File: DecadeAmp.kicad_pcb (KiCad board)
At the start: 2 copper layers, 60 x 60 mm, 30 parts, among them J1 Conn_Coaxial, J2 Conn_Coaxial, SW1 SS-24E06-TG 5 (P), U1 MCP6292-E/SN, U2 MCP6292-E/SN

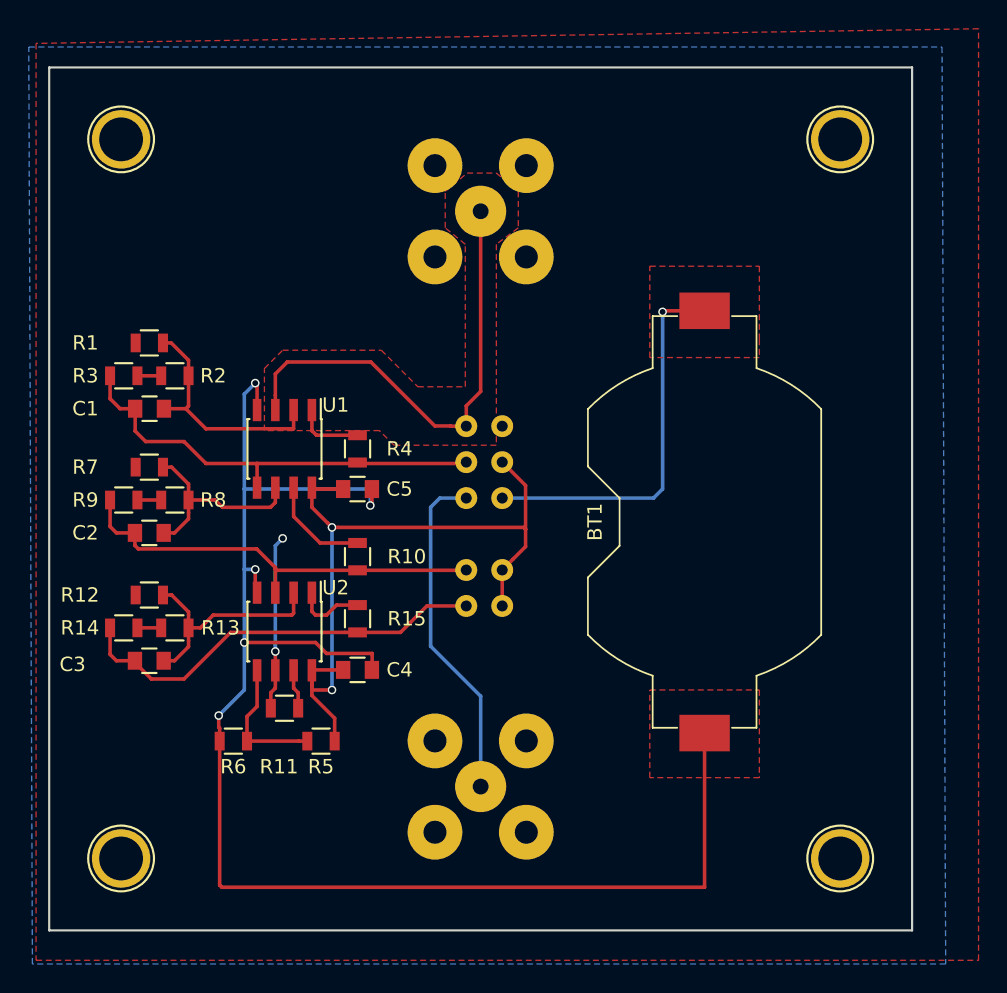
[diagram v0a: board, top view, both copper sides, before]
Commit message: moved to new packages
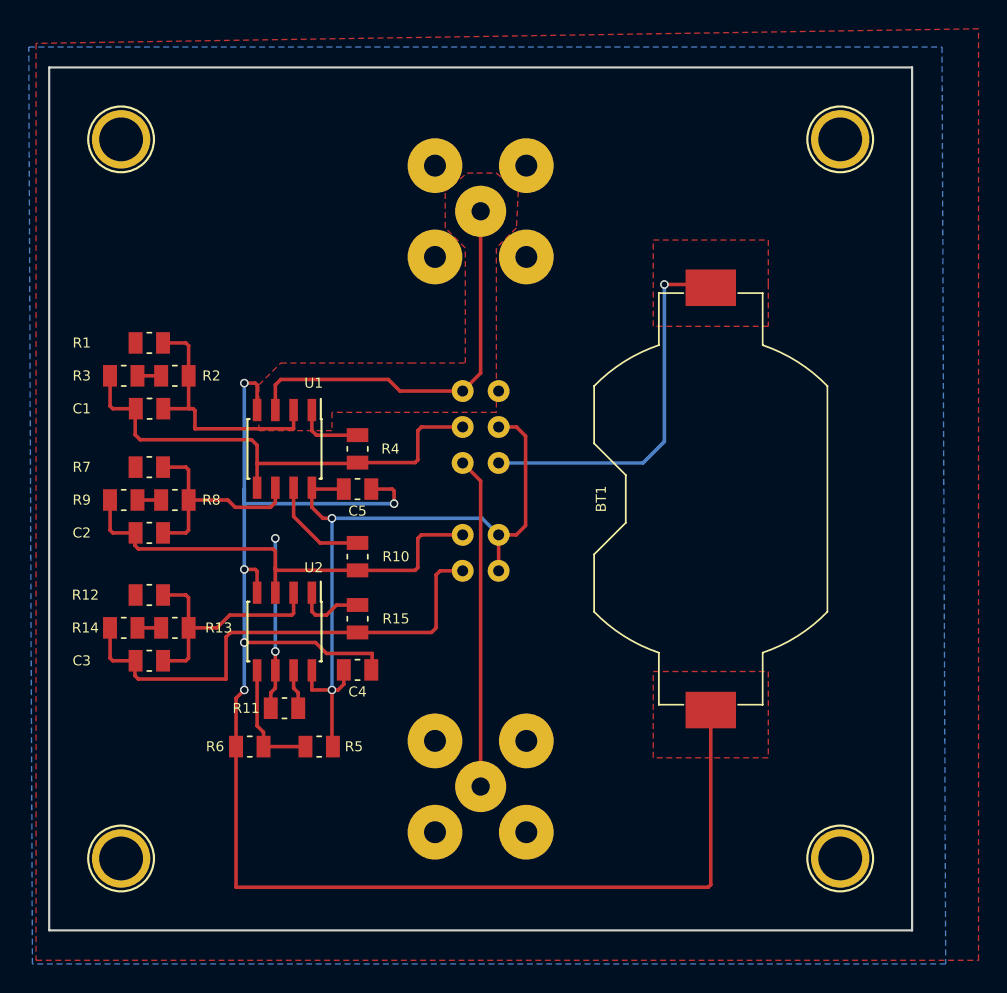
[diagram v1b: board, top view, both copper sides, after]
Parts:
- C1, C2, C3, C4, C5: footprint Capacitors_SMD:C_0805 -> Capacitor_SMD:C_0805_2012Metric
- J1, J2: footprint Connectors:bnc-ci -> Connector_Coaxial:BNC_TEConnectivity_1478204_Vertical
- R1, R10, R11, R12, R13, R14, R15, R2, R3, R4, R5, R6, R7, R8, R9: footprint Resistors_SMD:R_0805 -> Resistor_SMD:R_0805_2012Metric
- U1, U2: footprint Housings_SOIC:SOIC-8_3.9x4.9mm_Pitch1.27mm -> Package_SOIC:SOIC-8_3.9x4.9mm_P1.27mm
- moved SW1 2.45 mm to (101.2, 97.4)
- moved BT1 1.66 mm to (116.0, 100.0)
- moved R6 1.20 mm to (83.9, 117.2)
- moved R5 0.40 mm to (88.8, 117.2)
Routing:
- net /G_1000: track 29.5 -> 34.8 mm
- net /G_1: track 33.4 -> 28.4 mm
- net VEE: track 106.3 -> 109.9 mm
- net /G_10: track 31.0 -> 34.2 mm
- net /G_100: track 30.2 -> 33.0 mm
- net VCC: track 52.2 -> 50.6 mm
- net /FB10: track 16.6 -> 17.9 mm
- net /FB100: track 14.2 -> 15.3 mm
- net /FB1000: track 16.0 -> 17.0 mm
- net /VMID: track 9.41 -> 8.40 mm
- net /OUT: track 23.6 -> 23.0 mm, vias 1 -> 0
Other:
- board text added: "Selectable Decade Amplifier Ideas In Logic 2018 © Wolfgang Jung Rev. 1.0.1"
- board text added: "x1/OFF"
- board text removed: "Selectable Decade Amplifier Ideas In Logic 2018 © Wolfgang Jung Rev. 1.0.0"
- board text removed: "x1"

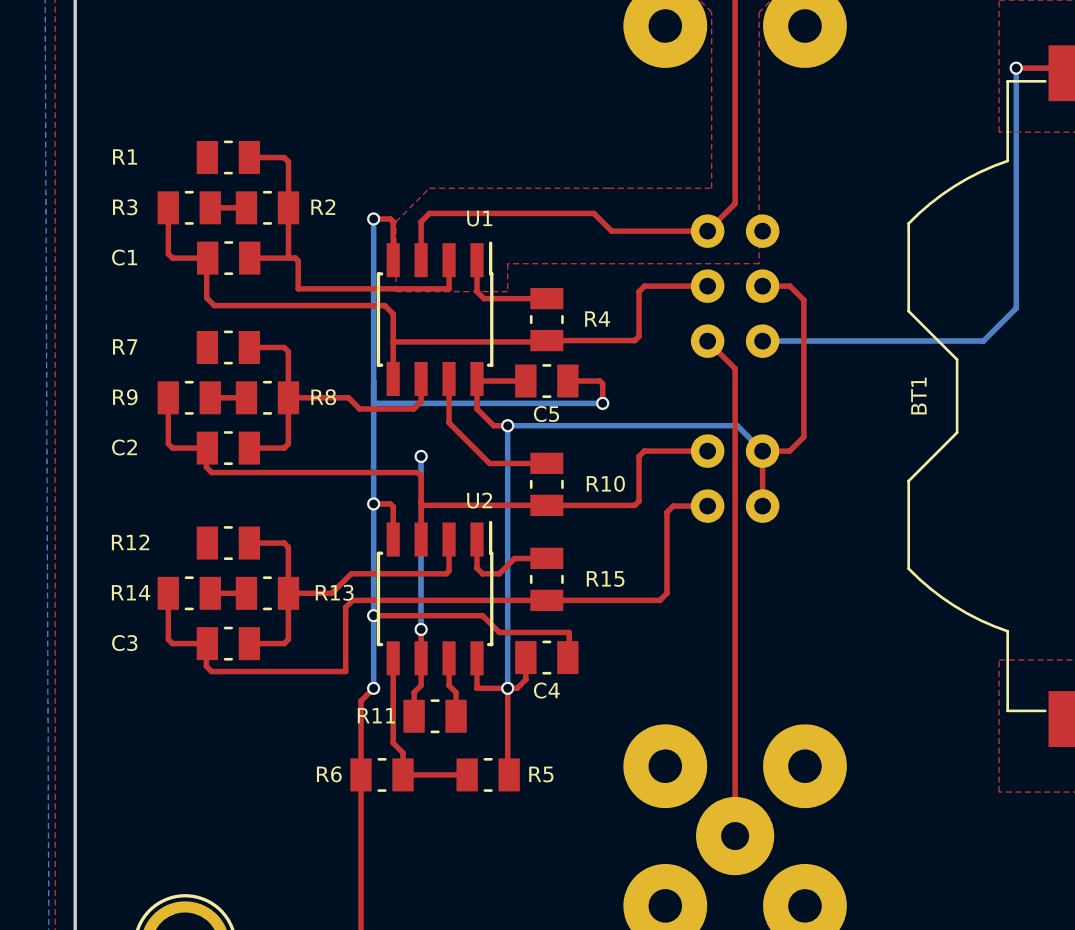
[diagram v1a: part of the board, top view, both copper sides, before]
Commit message: Better silkscreen, vendor-IDs of all components
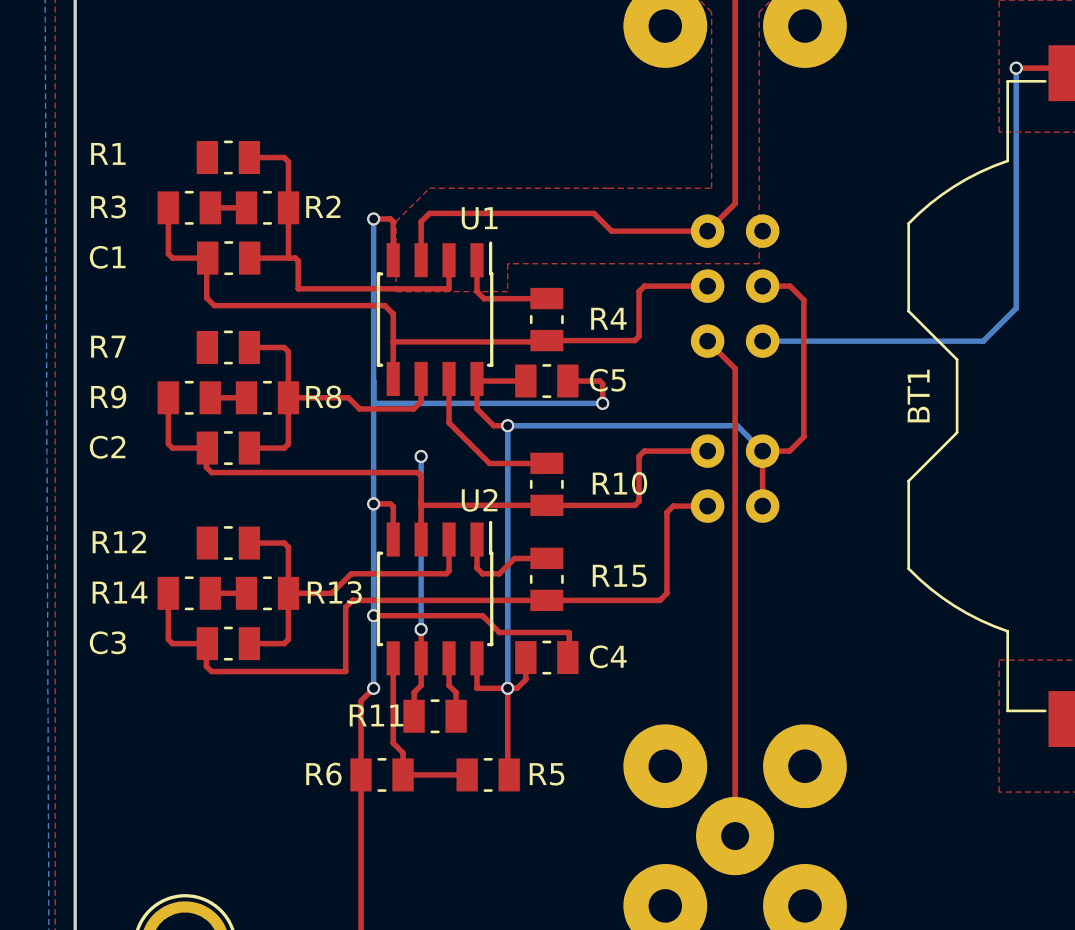
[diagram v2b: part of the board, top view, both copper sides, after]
